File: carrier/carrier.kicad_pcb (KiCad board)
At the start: 4 copper layers, 14 x 12 mm, 2 parts, among them J1 DF40GB-30DP-0.4V(51), U1 TC58NVG1S3HBAI6

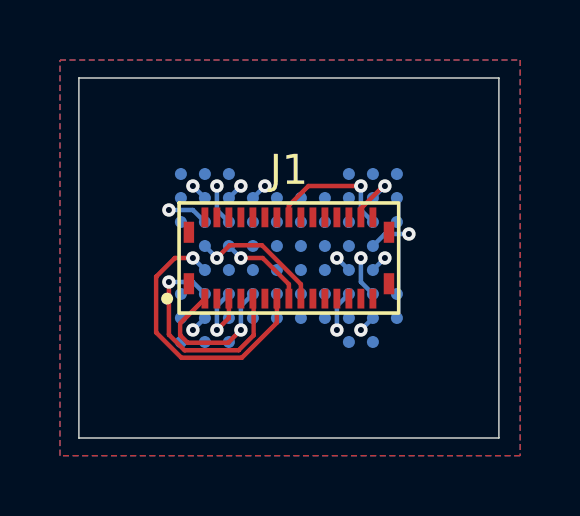
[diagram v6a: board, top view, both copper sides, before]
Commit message: Re-derive the J1 pinout from ball geometry; regenerate both schematics
Alex asked to optimise J1's pin assignment for the BGA fanout, and to
consider routing on the inner layers working back from J1 rather than
out from U1. Working backwards is what produced the result.

The topology falls out of the ball map with no slack. The VFBGA67's 20
used balls split into an upper cluster (columns 2-4: IO1-IO4 plus
CLE/RE/ALE/WP) and a lower one (columns 5-7: IO5-IO8, CE/WE/RY-BY and
both VCC balls) - exactly 8 and 7 signals. J1's odd row has exactly 8
signal slots and its even row exactly 7. So the row assignment is
forced, and within a row ordering by ball x makes the escape fan out
monotonically. IO1-IO8 are no longer in pin order on the connector;
that is deliberate and safe, because the rule that matters is the
end-to-end mapping, not the connector order.

Measured against the previous pinout with a routing-aware cost model
(octilinear where clear, around-the-end where the connector body is in
the way): 141.2 mm -> 74.8 mm of point-to-point routing, IO skew
10.32 mm -> 2.94 mm, and around-the-end paths 11 -> 5. Constraining the
bus to stay contiguous recovers almost none of that (139.6 mm), because
the IO balls all sit on one side while a monotonic bus spans J1's full
5.6 mm.

Skew was not the reason to do this. 10 mm is ~62 ps on FR4 against a
25 ns read cycle. The win is copper length and via count.

tools/pinout.py is now the single source: it carries the table and a
checker for the checkerboard invariant (no signal adjacent to or
opposite another signal) and the net set. Both schematics were
generated from it. Verified: carrier ERC 0, base ERC 0, both J1s match
the table, U1 matches the datasheet ball map, J2 matches the TSOP48
map, and IOn traces ball -> J1 pin -> TSOP48 pin end to end.

Carrier PCB carries placement, net re-import and the BGA escape (20/20
balls, DRC 0 errors). The J1 fanout is NOT routed in this commit - see
the next commit message / handoff for w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
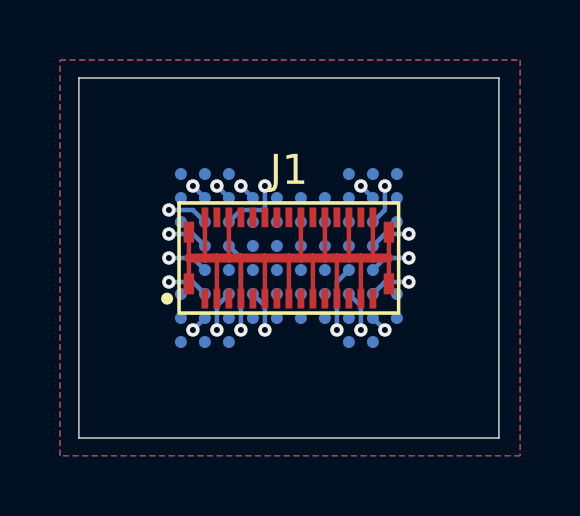
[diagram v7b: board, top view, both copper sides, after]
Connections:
- J1 pad 1: /IO1 -> /IO4
- J1 pad 10: GND -> VCC
- J1 pad 12: /ALE -> /IO8
- J1 pad 13: /IO4 -> /IO1
- J1 pad 14: GND -> VCC
- J1 pad 15: VCC -> GND
- J1 pad 16: //WE -> /IO6
- J1 pad 17: /IO5 -> /CLE
- J1 pad 19: VCC -> GND
- J1 pad 20: //RE -> /RY//BY
- J1 pad 21: /IO6 -> //RE
- J1 pad 24: //WP -> //WE
- J1 pad 25: /IO7 -> /ALE
- J1 pad 28: /RY//BY -> //CE
- J1 pad 29: /IO8 -> //WP
- J1 pad 4: //CE -> /IO7
- J1 pad 5: /IO2 -> /IO3
- J1 pad 8: /CLE -> /IO5
- J1 pad 9: /IO3 -> /IO2
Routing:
- net GND: track 1.70 -> 30.2 mm
- net /IO4: track 9.57 -> 1.37 mm
- net /IO3: track 7.60 -> 1.37 mm
- net /IO1: track 5.23 -> 1.37 mm
- net /IO5: track 4.56 -> 1.37 mm
- net //WE: track 4.43 -> 1.37 mm
- net VCC: track 6.31 -> 3.53 mm
- net /CLE: track 0.57 -> 2.17 mm
- net /RY//BY: track 1.97 -> 0.57 mm
- net /IO2: track 2.58 -> 1.37 mm
- net /IO6: track 1.37 -> 2.17 mm

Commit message: Carrier fully routed; propagate the VCC pin move to base and the docs
Alex routed the carrier: 0 DRC violations, 0 unconnected, one via per
signal net (20 total), uniform 0.15 mm tracks, teardrops on every
via/pad transition, GND poured on all four layers.

While routing he moved VCC from J1 pin 14 to pin 6, which is the right
call - pin 6's x lines up with the VCC ball H5, and pin 10 already lined
up with G7. But the change landed on the carrier only, so pin 6 was VCC
on one board and GND on the other, and pin 14 the reverse. Mated, that
is VCC shorted to GND through two pins.

Neither project can catch this: they are separate KiCad projects, so
each one's ERC and DRC pass happily. This is exactly the failure the
"single source of truth" note in the pinout doc exists to prevent.

Adopted the carrier's version as canonical: tools/pinout.py now has
VCC on 6 and 10, base regenerated from it, doc table updated. The
checkerboard invariant still holds. Verified both J1s now agree on all
34 pins including the G tabs.

carrier ERC 0, base ERC 0, carrier DRC 0 violations / 0 unconnected.

Co-Authored-By: Claude Opus 5 <noreply@anthropic.com>
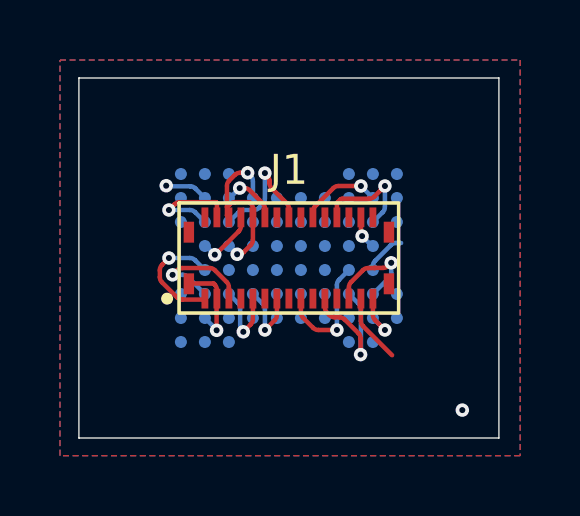
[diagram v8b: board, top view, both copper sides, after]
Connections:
- J1 pad 14: VCC -> GND
- J1 pad 6: GND -> VCC
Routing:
- net GND: track 30.2 -> 8.23 mm
- net //RE: track 1.37 -> 4.70 mm
- net VCC: track 3.53 -> 6.21 mm
- net /IO3: track 1.37 -> 3.97 mm
- net /IO4: track 1.37 -> 3.96 mm
- net //WE: track 1.37 -> 3.65 mm
- net /RY//BY: track 0.57 -> 2.75 mm
- net /IO7: track 1.37 -> 3.54 mm
- net /ALE: track 1.37 -> 3.43 mm
- net /IO6: track 2.17 -> 4.17 mm
- net /CLE: track 2.17 -> 4.09 mm
- net /IO8: track 0.57 -> 1.95 mm
- net /IO2: track 1.37 -> 2.66 mm
- net //WP: track 0.57 -> 1.76 mm
- net /IO1: track 1.37 -> 2.55 mm
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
